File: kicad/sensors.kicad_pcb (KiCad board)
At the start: 2 copper layers, 84.6 x 64 mm, 52 parts, among them J1 Bus_PCI_Express_x1, J4 Conn_01x02, J6 USB_C_Receptacle_USB2.0_16P, U2 RP2040, U4 W25Q128JVP, U5 BMP388, U8 BNO055, U9 MCP25625T-E/ML, X1 ABM8-272-T3, Y1 ABS07-32.768KHZ-T, Y2 X322516MLB4SI

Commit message: Update board to 0.2.0
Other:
- board size 84.6 x 64 mm -> 84.1 x 61.7 mm
- board text added: "sensors 0.2.0"
- board text removed: "sensors 0.1.0"

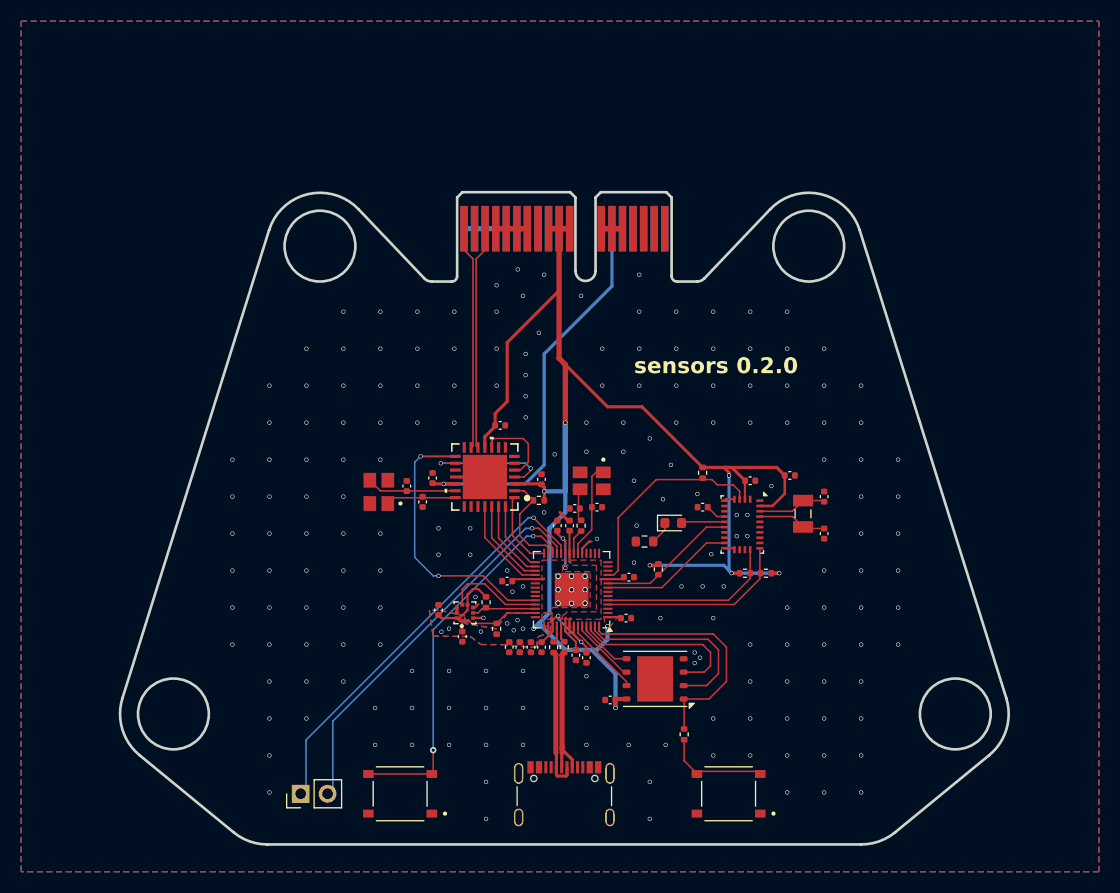
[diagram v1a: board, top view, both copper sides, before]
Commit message: add USBC resistors, power status LEDs, silk screen indicator, change SPI pins
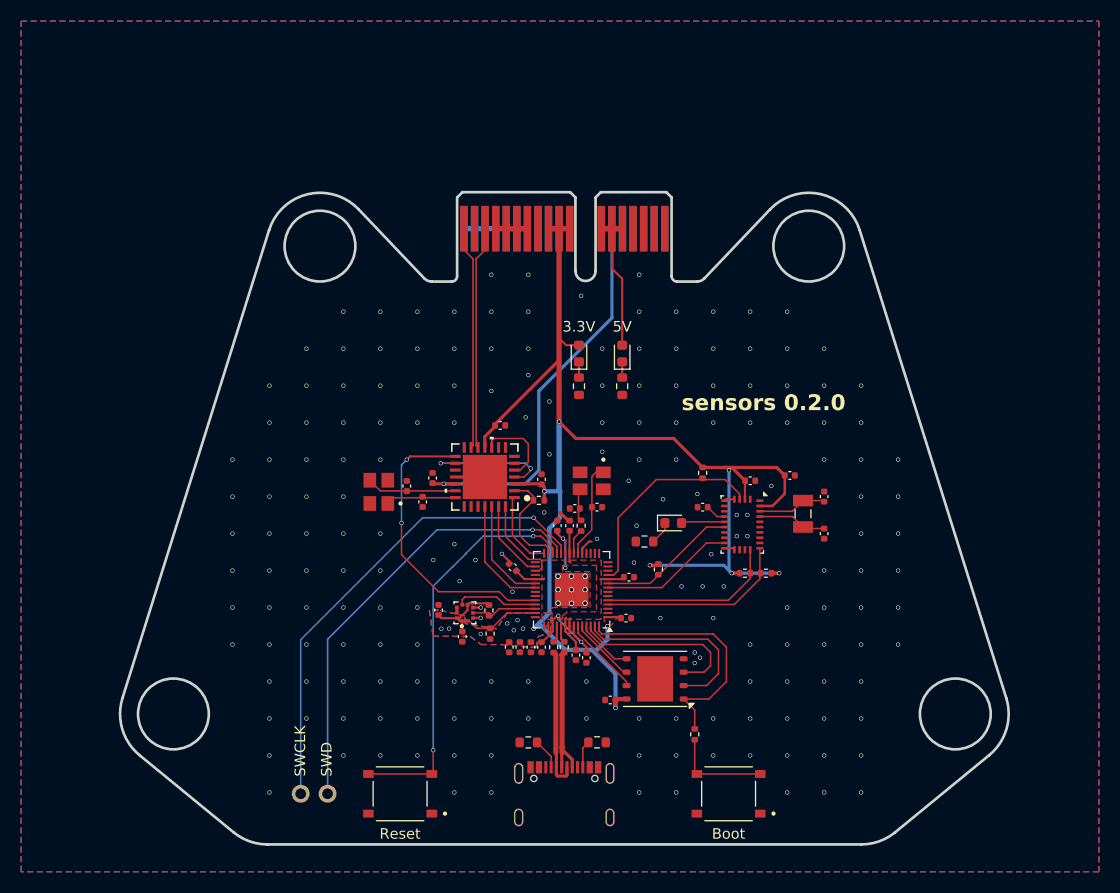
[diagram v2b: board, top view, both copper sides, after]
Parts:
- added D1: LED, LED_SMD:LED_0603_1608Metric, F.Cu at (147.8, 76.0)
- added D2: LED, LED_SMD:LED_0603_1608Metric, F.Cu at (151.9, 76.0)
- added R1: 150, Resistor_SMD:R_0603_1608Metric, F.Cu at (147.8, 79.1)
- added R2: 150, Resistor_SMD:R_0603_1608Metric, F.Cu at (151.9, 79.1)
- added R3: 5.1k, Resistor_SMD:R_0603_1608Metric, F.Cu at (149.5, 112.8)
- added R4: 5.1k, Resistor_SMD:R_0603_1608Metric, F.Cu at (143.0, 112.8)
- moved C212 1.41 mm to (141.5, 96.2), turned to 135 degrees
- moved R30 1.00 mm to (158.8, 112.0)
- moved R223 0.82 mm to (139.3, 100.3)
- moved R222 0.77 mm to (139.4, 102.5)
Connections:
- J1 pad A16: +7.4V -> unconnected-(J1-PERp0-PadA16)
- J1 pad A17: +7.4V -> unconnected-(J1-PERn0-PadA17)
- J1 pad A18: +7.4V -> unconnected-(J1-GND-PadA18)
- J1 pad B16: +7.4V -> unconnected-(J1-GND-PadB16)
- J1 pad B17: +7.4V -> unconnected-(J1-~{PRSNT2}-PadB17)
- J1 pad B18: +7.4V -> unconnected-(J1-GND-PadB18)
- J6 pad A5: unconnected-(J6-CC1-PadA5) -> Net-(J6-CC1)
- J6 pad B5: unconnected-(J6-CC2-PadB5) -> Net-(J6-CC2)
- U2 pad 29: SO -> unconnected-(U2-GPIO18-Pad29)
- U2 pad 31: SCK -> SO
- U2 pad 32: CANINT -> unconnected-(U2-GPIO21-Pad32)
- U2 pad 34: unconnected-(U2-GPIO22-Pad34) -> SCK
- U2 pad 35: unconnected-(U2-GPIO23-Pad35) -> CANINT
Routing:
- net +5V: track 41.2 -> 52.6 mm
- net /SWCLK: track 40.0 -> 45.9 mm
- net /SWD: track 37.2 -> 41.8 mm
- net Net-(J6-CC1): track 0.00 -> 2.90 mm
- net Net-(J6-CC2): track 0.00 -> 2.58 mm
- net /RUN: track 35.6 -> 38.0 mm
- net CANSTBY: track 26.2 -> 28.4 mm
- net SO: track 6.71 -> 8.62 mm
- net CANINT: track 9.18 -> 11.0 mm
- net +3.3V: track 168.2 -> 166.5 mm
- net SCK: track 8.38 -> 10.1 mm
- net BMPINT: track 9.42 -> 7.80 mm
- net Net-(D2-K): track 0.00 -> 1.49 mm
- net Net-(D1-K): track 0.00 -> 1.49 mm
- net GND: track 19.1 -> 20.2 mm, vias 202 -> 203
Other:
- board text added: "3.3V"
- board text added: "5V"
- board text added: "Boot"
- board text added: "Reset"
- board text added: "SWCLK"
- board text added: "SWD"

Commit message: update BOM, generate new production files
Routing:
- net GND: vias 203 -> 201
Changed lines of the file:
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@@
 		(attr smd)
 		(fp_line
-			(start 0.8 -0.735)
-			(end -1.485 -0.735)
-			(stroke
-				(width 0.12)
-				(type solid)
-			)
-			(layer "F.SilkS")
-		)
-		(fp_line
-			(start -1.485 -0.735)
-			(end -1.485 0.735)
-			(stroke
-				(width 0.12)
-				(type solid)
-			)
-			(layer "F.SilkS")
-		)
-		(fp_line
-			(start -1.485 0.735)
-			(end 0.8 0.735)
-			(stroke
-				(width 0.12)
-				(type solid)
-			)
-			(layer "F.SilkS")
-		)
-		(fp_line
 			(start 1.48 -0.73)
 			(end 1.48 0.73)
@@
 			(layer "F.Fab")
 		)
+		(fp_text user "-"
+			(at -1.439612 1.695543 90)
+			(unlocked yes)
+			(layer "F.SilkS")
+			(effects
+				(font
+					(size 1 1)
+					(thickness 0.1)
+				)
+				(justify left bottom)
+			)
+		)
+		(fp_text user "+"
+			(at 0.119967 1.719536 90)
+			(unlocked yes)
+			(layer "F.SilkS")
+			(effects
+				(font
+					(size 1 1)
+					(thickness 0.1)
+				)
+				(justify left bottom)
+			)
+		)
 		(fp_text user "${REFERENCE}"
 			(at 0 0 90)
@@
 		(attr smd)
 		(fp_line
-			(start -1.485 -0.735)
-			(end -1.485 0.735)
-			(stroke
-				(width 0.12)
-				(type solid)
-			)
-			(layer "F.SilkS")
-		)
-		(fp_line
-			(start -1.485 0.735)
-			(end 0.8 0.735)
-			(stroke
-				(width 0.12)
-				(type solid)
-			)
-			(layer "F.SilkS")
-		)
-		(fp_line
-			(start 0.8 -0.735)
-			(end -1.485 -0.735)
-			(stroke
-				(width 0.12)
-				(type solid)
-			)
-			(layer "F.SilkS")
-		)
-		(fp_line
 			(start -1.48 -0.73)
 			(end 1.48 -0.73)
@@
 			(layer "F.Fab")
 		)
+		(fp_text user "-"
+			(at -1.439612 -0.5 0)
+			(unlocked yes)
+			(layer "F.SilkS")
+			(effects
+				(font
+					(size 1 1)
+					(thickness 0.1)
+				)
+				(justify left bottom)
+			)
+		)
+		(fp_text user "+"
+			(at 0 -0.73 0)
+			(unlocked yes)
+			(layer "F.SilkS")
+			(effects
+				(font
+					(size 1 1)
+					(thickness 0.1)
+				)
+				(justify left bottom)
+			)
+		)
 		(fp_text user "${REFERENCE}"
 			(at 0 0 0)
@@
 		(attr smd)
 		(fp_line
-			(start 0.8 -0.735)
-			(end -1.485 -0.735)
-			(stroke
-				(width 0.12)
-				(type solid)
-			)
-			(layer "F.SilkS")
-		)
-		(fp_line
-			(start -1.485 -0.735)
-			(end -1.485 0.735)
-			(stroke
-				(width 0.12)
-				(type solid)
-			)
-			(layer "F.SilkS")
-		)
-		(fp_line
-			(start -1.485 0.735)
-			(end 0.8 0.735)
-			(stroke
-				(width 0.12)
-				(type solid)
-			)
-			(layer "F.SilkS")
-		)
-		(fp_line
 			(start 1.48 -0.73)
 			(end 1.48 0.73)
@@
 			(layer "F.Fab")
 		)
+		(fp_text user "+"
+			(at 0.145403 1.773387 90)
+			(unlocked yes)
+			(layer "F.SilkS")
+			(effects
+				(font
+					(size 1 1)
+					(thickness 0.1)
+				)
+				(justify left bottom)
+			)
+		)
+		(fp_text user "-"
+			(at -1.5 1.744752 90)
+			(unlocked yes)
+			(layer "F.SilkS")
+			(effects
+				(font
+					(size 1 1)
+					(thickness 0.1)
+				)
+				(justify left bottom)
+			)
+		)
 		(fp_text user "${REFERENCE}"
 			(at 0 0 90)
@@
 	)
 	(footprint "Connector_PCBEdge:BUS_PCIexpress_x1"
+		(locked yes)
 		(layer "B.Cu")
 		(at 136.913 64.138595)
@@
 		(start 159.678146 68.835513)
 		(end 165.883818 62.312636)
+		(locked yes)
 		(stroke
 			(width 0.25)
@@
 		(start 133.143972 68.831791)
 		(end 126.941843 62.312637)
+		(locked yes)
 		(stroke
 			(width 0.25)
@@
 		(start 174.511605 122.419976)
 		(end 118.31403 122.419976)
+		(locked yes)
 		(stroke
 			(width 0.25)
@@
 		(center 183.413305 110.068595)
 		(end 180.063305 110.068595)
+		(locked yes)
 		(stroke
 			(width 0.25)
@@
 		(mid 159.347804 69.065283)
 		(end 158.95364 69.146243)
+		(locked yes)
 		(stroke
 			(width 0.25)
@@
 		(mid 188.252259 111.513246)
 		(end 186.615928 113.973169)
+		(locked yes)
 		(stroke
 			(width 0.25)
@@
 		(start 133.87203 69.146243)
 		(end 135.755183 69.146243)
+		(locked yes)
 		(stroke
 			(width 0.25)
@@
 		(mid 116.613396 122.125003)
 		(end 115.111431 121.274551)
+		(locked yes)
 		(stroke
 			(width 0.25)
@@
 		(start 158.95364 69.146243)
 		(end 157.070478 69.146243)
+		(locked yes)
 		(stroke
 			(width 0.25)
@@
 		(start 174.361605 64.283721)
 		(end 174.361606 64.283721)
+		(locked yes)
 		(stroke
 			(width 0.25)
@@
 		(start 186.615928 113.973169)
 		(end 177.714231 121.274549)
+		(locked yes)
 		(stroke
 			(width 0.25)
@@
 		(mid 133.475493 69.064276)
 		(end 133.143972 68.831791)
+		(locked yes)
 		(stroke
 			(width 0.25)
@@
 		(mid 170.686181 60.874652)
 		(end 174.361605 64.283721)
+		(locked yes)
 		(stroke
 			(width 0.25)
@@
 		(mid 122.13948 60.874652)
 		(end 126.941843 62.312637)
+		(locked yes)
 		(stroke
 			(width 0.25)
@@
 		(center 109.412355 110.068595)
 		(end 106.062355 110.068595)
+		(locked yes)
 		(stroke
 			(width 0.25)
@@
 		(mid 136.108734 68.999813)
 		(end 135.755183 69.146243)
+		(locked yes)
 		(stroke
 			(width 0.25)
@@
 		(start 174.361606 64.283721)
 		(end 188.23235 108.558858)
+		(locked yes)
 		(stroke
 			(width 0.25)
@@
 		(center 169.54256 65.793456)
 		(end 166.19256 65.793456)
+		(locked yes)
 		(stroke
 			(width 0.25)
@@
 		(center 123.2831 65.793456)
 		(end 119.9331 65.793456)
+		(locked yes)
 		(stroke
 			(width 0.25)
@@
 		(start 106.209767 113.973198)
 		(end 115.111431 121.274551)
+		(locked yes)
 		(stroke
 			(width 0.25)
@@
 		(start 118.464055 64.28372)
 		(end 118.464054 64.28372)
+		(locked yes)
 		(stroke
 			(width 0.25)
@@
 		(mid 156.716924 68.999796)
 		(end 156.570477 68.646242)
+		(locked yes)
 		(stroke
 			(width 0.25)
@@
 		(start 118.464054 64.28372)
 		(end 104.588376 108.574607)
+		(locked yes)
 		(stroke
 			(width 0.25)
@@
 		(mid 104.575789 111.521169)
 		(end 104.588376 108.574607)
+		(locked yes)
 		(stroke
 			(width 0.25)
@@
 		(mid 176.212253 122.125005)
 		(end 174.511605 122.419976)
+		(locked yes)
 		(stroke
 			(width 0.25)
@@
 	)
 	(via
-		(at 167.5 72)
-		(size 0.4)
-		(drill 0.3)
-		(layers "F.Cu" "B.Cu")
-		(free yes)
-		(net 25)
-	)
-	(via
 		(at 125.5 93)
 		(size 0.4)
@@
 		(size 0.4)
 		(drill 0.3)
-		(layers "F.Cu" "B.Cu")
-		(free yes)
-		(net 25)
-	)
-	(via
-		(at 125.5 72)
-		(size 0.4)
-		(drill 0.3)

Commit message: finalize board, update production files
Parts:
- R3, R4: footprint Resistor_SMD:R_0603_1608Metric -> Resistor_SMD:R_0402_1005Metric
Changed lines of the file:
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@@
 		)
 	)
-	(footprint "Resistor_SMD:R_0603_1608Metric"
+	(footprint "Resistor_SMD:R_0402_1005Metric"
 		(layer "F.Cu")
 		(at 143.005 112.765)
-		(descr "Resistor SMD 0603 (1608 Metric), square (rectangular) end terminal, IPC_7351 nominal, (Body size source: IPC-SM-782 page 72, https://www.pcb-3d.com/wordpress/wp-content/uploads/ipc-sm-782a_amendment_1_and_2.pdf), generated with kicad-footprint-generator")
+		(descr "Resistor SMD 0402 (1005 Metric), square (rectangular) end terminal, IPC_7351 nominal, (Body size source: IPC-SM-782 page 72, https://www.pcb-3d.com/wordpress/wp-content/uploads/ipc-sm-782a_amendment_1_and_2.pdf), generated with kicad-footprint-generator")
 		(tags "resistor")
 		(property "Reference" "R4"
-			(at 0 -1.43 0)
+			(at 0 -1.17 0)
 			(layer "F.SilkS")
 			(hide yes)
@@
 		)
 		(property "Value" "5.1k"
-			(at 0 1.43 0)
+			(at 0 1.17 0)
 			(layer "F.Fab")
+			(hide yes)
 			(effects
 				(font
@@
 			)
 		)
-		(property "Footprint" "Resistor_SMD:R_0603_1608Metric"
+		(property "Footprint" "Resistor_SMD:R_0402_1005Metric"
 			(at 0 0 0)
 			(unlocked yes)
@@
 			)
 		)
-		(property "JLC Link" "https://jlcpcb.com/partdetail/23535-0603WAF1500T5E/C22808"
+		(property "JLC Link" "https://jlcpcb.com/partdetail/26648-0402WGF5101TCE/C25905"
 			(at 0 0 0)
 			(unlocked yes)
@@
 			)
 		)
-		(property "LCSC Part #" "C22808"
+		(property "LCSC Part #" "C25905"
 			(at 0 0 0)
 			(unlocked yes)
@@
 			)
 		)
-		(property "info" "150 ohm"
+		(property "info" "5.1k ohm"
 			(at 0 0 0)
 			(unlocked yes)
@@
 			)
 		)
-		(property "price" "C$0.0013 "
+		(property "price" "C$0.0006"
 			(at 0 0 0)
 			(unlocked yes)
@@
 		(attr smd)
 		(fp_line
-			(start -0.237258 -0.5225)
-			(end 0.237258 -0.5225)
+			(start -0.153641 -0.38)
+			(end 0.153641 -0.38)
 			(stroke
 				(width 0.12)
@@
 		)
 		(fp_line
-			(start -0.237258 0.5225)
-			(end 0.237258 0.5225)
+			(start -0.153641 0.38)
+			(end 0.153641 0.38)
 			(stroke
 				(width 0.12)
@@
 		)
 		(fp_line
-			(start -1.48 -0.73)
-			(end 1.48 -0.73)
+			(start -0.93 -0.47)
+			(end 0.93 -0.47)
 			(stroke
 				(width 0.05)
@@
 		)
 		(fp_line
-			(start -1.48 0.73)
-			(end -1.48 -0.73)
+			(start -0.93 0.47)
+			(end -0.93 -0.47)
 			(stroke
 				(width 0.05)
@@
 		)
 		(fp_line
-			(start 1.48 -0.73)
-			(end 1.48 0.73)
+			(start 0.93 -0.47)
+			(end 0.93 0.47)
 			(stroke
 				(width 0.05)
@@
 		)
 		(fp_line
-			(start 1.48 0.73)
-			(end -1.48 0.73)
+			(start 0.93 0.47)
+			(end -0.93 0.47)
 			(stroke
 				(width 0.05)
@@
 		)
 		(fp_line
-			(start -0.8 -0.4125)
-			(end 0.8 -0.4125)
+			(start -0.525 -0.27)
+			(end 0.525 -0.27)
 			(stroke
 				(width 0.1)
@@
 		)
 		(fp_line
-			(start -0.8 0.4125)
-			(end -0.8 -0.4125)
+			(start -0.525 0.27)
+			(end -0.525 -0.27)
 			(stroke
 				(width 0.1)
@@
 		)
 		(fp_line
-			(start 0.8 -0.4125)
-			(end 0.8 0.4125)
+			(start 0.525 -0.27)
+			(end 0.525 0.27)
 			(stroke
 				(width 0.1)
@@
 		)
 		(fp_line
-			(start 0.8 0.4125)
-			(end -0.8 0.4125)
+			(start 0.525 0.27)
+			(end -0.525 0.27)
 			(stroke
 				(width 0.1)
@@
 			(effects
 				(font
-					(size 0.4 0.4)
-					(thickness 0.06)
+					(size 0.26 0.26)
+					(thickness 0.04)
 				)
 			)
 		)
 		(pad "1" smd roundrect
-			(at -0.825 0)
-			(size 0.8 0.95)
+			(at -0.51 0)
+			(size 0.54 0.64)
 			(layers "F.Cu" "F.Paste" "F.Mask")
 			(roundrect_rratio 0.25)
@@
 		)
 		(pad "2" smd roundrect
-			(at 0.825 0)
-			(size 0.8 0.95)
+			(at 0.51 0)
+			(size 0.54 0.64)
 			(layers "F.Cu" "F.Paste" "F.Mask")
 			(roundrect_rratio 0.25)
@@
 			(pintype "passive")
 		)
-		(model "${KICAD8_3DMODEL_DIR}/Resistor_SMD.3dshapes/R_0603_1608Metric.wrl"
+		(model "${KICAD8_3DMODEL_DIR}/Resistor_SMD.3dshapes/R_0402_1005Metric.wrl"
 			(offset
 				(xyz 0 0 0)
@@
 		)
 	)
-	(footprint "Resistor_SMD:R_0603_1608Metric"
+	(footprint "Resistor_SMD:R_0402_1005Metric"
 		(layer "F.Cu")
 		(at 149.505 112.755)
-		(descr "Resistor SMD 0603 (1608 Metric), square (rectangular) end terminal, IPC_7351 nominal, (Body size source: IPC-SM-782 page 72, https://www.pcb-3d.com/wordpress/wp-content/uploads/ipc-sm-782a_amendment_1_and_2.pdf), generated with kicad-footprint-generator")
+		(descr "Resistor SMD 0402 (1005 Metric), square (rectangular) end terminal, IPC_7351 nominal, (Body size source: IPC-SM-782 page 72, https://www.pcb-3d.com/wordpress/wp-content/uploads/ipc-sm-782a_amendment_1_and_2.pdf), generated with kicad-footprint-generator")
 		(tags "resistor")
 		(property "Reference" "R3"
-			(at 0 -1.43 0)
+			(at 0 -1.17 0)
 			(layer "F.SilkS")
 			(hide yes)
@@
 		)
 		(property "Value" "5.1k"
-			(at 0 1.43 0)
+			(at 0 1.17 0)
 			(layer "F.Fab")
+			(hide yes)
 			(effects
 				(font
@@
 			)
 		)
-		(property "Footprint" "Resistor_SMD:R_0603_1608Metric"
+		(property "Footprint" "Resistor_SMD:R_0402_1005Metric"
 			(at 0 0 0)
 			(unlocked yes)
@@
 			)
 		)
-		(property "JLC Link" "https://jlcpcb.com/partdetail/23535-0603WAF1500T5E/C22808"
+		(property "JLC Link" "https://jlcpcb.com/partdetail/26648-0402WGF5101TCE/C25905"
 			(at 0 0 0)
 			(unlocked yes)
@@
 			)
 		)
-		(property "LCSC Part #" "C22808"
+		(property "LCSC Part #" "C25905"
 			(at 0 0 0)
 			(unlocked yes)
@@
 			)
 		)
-		(property "info" "150 ohm"
+		(property "info" "5.1k ohm"
 			(at 0 0 0)
 			(unlocked yes)
@@
 			)
 		)
-		(property "price" "C$0.0013 "
+		(property "price" "C$0.0006"
 			(at 0 0 0)
 			(unlocked yes)
@@
 		(attr smd)
 		(fp_line
-			(start -0.237258 -0.5225)
-			(end 0.237258 -0.5225)
+			(start -0.153641 -0.38)
+			(end 0.153641 -0.38)
 			(stroke
 				(width 0.12)
@@
 		)
 		(fp_line
-			(start -0.237258 0.5225)
-			(end 0.237258 0.5225)
+			(start -0.153641 0.38)
+			(end 0.153641 0.38)
 			(stroke
 				(width 0.12)
@@
 		)
 		(fp_line
-			(start -1.48 -0.73)
-			(end 1.48 -0.73)
+			(start -0.93 -0.47)
+			(end 0.93 -0.47)
 			(stroke
 				(width 0.05)
@@
 		)
 		(fp_line
-			(start -1.48 0.73)
-			(end -1.48 -0.73)
+			(start -0.93 0.47)
+			(end -0.93 -0.47)
 			(stroke
 				(width 0.05)
@@
 		)
 		(fp_line
-			(start 1.48 -0.73)
-			(end 1.48 0.73)
+			(start 0.93 -0.47)
+			(end 0.93 0.47)
 			(stroke
 				(width 0.05)
@@
 		)
 		(fp_line
-			(start 1.48 0.73)
-			(end -1.48 0.73)
+			(start 0.93 0.47)
+			(end -0.93 0.47)
 			(stroke
 				(width 0.05)
@@
 		)
 		(fp_line
-			(start -0.8 -0.4125)
-			(end 0.8 -0.4125)
+			(start -0.525 -0.27)
+			(end 0.525 -0.27)
 			(stroke
 				(width 0.1)
@@
 		)
 		(fp_line
-			(start -0.8 0.4125)
-			(end -0.8 -0.4125)
+			(start -0.525 0.27)
+			(end -0.525 -0.27)
 			(stroke
 				(width 0.1)
@@
 		)
 		(fp_line
-			(start 0.8 -0.4125)
-			(end 0.8 0.4125)
+			(start 0.525 -0.27)
+			(end 0.525 0.27)
 			(stroke
 				(width 0.1)
@@
 		)
 		(fp_line
-			(start 0.8 0.4125)
-			(end -0.8 0.4125)
+			(start 0.525 0.27)
+			(end -0.525 0.27)
 			(stroke
 				(width 0.1)
@@
 			(effects
 				(font
-					(size 0.4 0.4)
-					(thickness 0.06)
+					(size 0.26 0.26)
+					(thickness 0.04)
 				)
 			)
 		)
 		(pad "1" smd roundrect
-			(at -0.825 0)
-			(size 0.8 0.95)
+			(at -0.51 0)
+			(size 0.54 0.64)
 			(layers "F.Cu" "F.Paste" "F.Mask")
 			(roundrect_rratio 0.25)
@@
 		)
 		(pad "2" smd roundrect
-			(at 0.825 0)
-			(size 0.8 0.95)
+			(at 0.51 0)
+			(size 0.54 0.64)
 			(layers "F.Cu" "F.Paste" "F.Mask")
 			(roundrect_rratio 0.25)
@@
 			(pintype "passive")
 		)
-		(model "${KICAD8_3DMODEL_DIR}/Resistor_SMD.3dshapes/R_0603_1608Metric.wrl"
+		(model "${KICAD8_3DMODEL_DIR}/Resistor_SMD.3dshapes/R_0402_1005Metric.wrl"
 			(offset
 				(xyz 0 0 0)
@@
 	(segment
 		(start 148.16 115.115)
-		(end 148.16 113.275)
+		(end 148.16 113.59)
 		(width 0.15)
 		(layer "F.Cu")
@@
 	)
 	(segment
-		(start 148.16 113.275)
-		(end 148.68 112.755)
+		(start 148.16 113.59)
+		(end 148.995 112.755)
 		(width 0.15)
 		(layer "F.Cu")
@@
 	)
 	(segment
-		(start 145.16 114.095)
-		(end 143.83 112.765)
+		(start 145.16 115.115)
+		(end 145.16 114.41)
 		(width 0.15)
 		(layer "F.Cu")
@@
 	)
 	(segment
-		(start 145.16 115.115)
-		(end 145.16 114.095)
+		(start 145.16 114.41)
+		(end 143.515 112.765)
 		(width 0.15)
 		(layer "F.Cu")
